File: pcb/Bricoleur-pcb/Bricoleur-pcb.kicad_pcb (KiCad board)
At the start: 2 copper layers, 74 parts, among them J1 USB_B_Micro, J2 Conn_02x10_Odd_Even, J3 Conn_02x03_Odd_Even, J4 Conn_02x03_Odd_Even, SW2 SW_Push, SW3 SW_Push, SW4 SW_Push, SW5 SW_Push, U1 Ultrasonic-LV-EZ0, U11 SW_DP3T, U2 PYNQ-Shield-Bricoleur-pcb-cac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, U3 Ultrasonic-LV-EZ0, U4 Ultrasonic-LV-EZ0, U5 Arducam-OV5642, U6 Arducam-OV5642, U7 EFM32GG980, U8 UART_BOOT, U9 IP4220CZ6

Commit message: Narrowed down component placement, continued routing
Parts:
- moved TP1 239.7 mm to (86.3, 158.6)
- moved U11 189.6 mm to (77.7, 141.9)
- moved C14 147.8 mm to (44.2, 155.6), turned to 90 degrees
- moved C15 142.5 mm to (60.4, 155.6), turned to 90 degrees
- moved C13 138.9 mm to (47.3, 109.4), turned to 180 degrees
- moved C16 138.0 mm to (77.7, 155.6), turned to 90 degrees
- moved L1 135.5 mm to (99.0, 90.1)
- moved J1 133.3 mm to (98.9, 95.3), turned to 270 degrees
- moved U9 129.6 mm to (104.1, 88.0)
- moved R4 121.2 mm to (68.1, 150.0), turned to 180 degrees
- moved C7 118.8 mm to (62.0, 126.1), turned to 270 degrees
- moved C9 117.2 mm to (56.4, 126.1), turned to 270 degrees
- moved C10 116.4 mm to (48.3, 111.4), turned to 180 degrees
- moved C3 111.8 mm to (57.9, 126.1), turned to 90 degrees
- moved R17 109.7 mm to (92.4, 143.4), turned to 270 degrees
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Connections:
- net Net-(J1-Pad2) renamed /USB_D-
- net Net-(J1-Pad3) renamed /USB_D+
- J1 pad 4: (no net) -> Net-(J1-Pad4)
- J2 pad 2: (no net) -> Net-(J2-Pad2)
- J2 pad 3: (no net) -> Net-(J2-Pad3)
- J2 pad 5: (no net) -> Net-(J2-Pad5)
- J3 pad 1: /US0_CLK -> /US0_TX
- J3 pad 5: /US0_TX -> /US0_CLK
- J4 pad 1: /US1_CLK -> /US1_TX
- J4 pad 5: /US1_TX -> /US1_CLK
- U1 pad 2: (no net) -> Net-(U1-Pad2)
- U1 pad 4: (no net) -> Net-(U1-Pad4)
- U2 pad 1: (no net) -> Net-(U2-Pad1)
- U2 pad 10: (no net) -> Net-(U2-Pad10)
- U2 pad 11: (no net) -> Net-(U2-Pad11)
- U2 pad 12: (no net) -> Net-(U2-Pad12)
- U2 pad 13: (no net) -> Net-(U2-Pad13)
- U2 pad 14: (no net) -> Net-(U2-Pad14)
- U2 pad 15: (no net) -> Net-(U2-Pad15)
- U2 pad 16: (no net) -> Net-(U2-Pad16)
- U2 pad 17: (no net) -> Net-(U2-Pad17)
- U2 pad 18: (no net) -> Net-(U2-Pad18)
- U2 pad 19: (no net) -> Net-(U2-Pad19)
- U2 pad 2: (no net) -> Net-(U2-Pad2)
- U2 pad 20: (no net) -> Net-(U2-Pad20)
- U2 pad 21: (no net) -> Net-(U2-Pad21)
- U2 pad 22: (no net) -> Net-(U2-Pad22)
- U2 pad 23: (no net) -> Net-(U2-Pad23)
- U2 pad 24: (no net) -> Net-(U2-Pad24)
- U2 pad 25: (no net) -> Net-(U2-Pad25)
- U2 pad 26: (no net) -> Net-(U2-Pad26)
- U2 pad 28: (no net) -> Net-(U2-Pad28)
- U2 pad 3: (no net) -> Net-(U2-Pad3)
- U2 pad 34: (no net) -> Net-(U2-Pad34)
- U2 pad 5: (no net) -> /PYNQ_5V0
- U2 pad 8: (no net) -> Net-(U2-Pad8)
- U2 pad 9: (no net) -> Net-(U2-Pad9)
- U3 pad 2: (no net) -> Net-(U3-Pad2)
- U3 pad 4: (no net) -> Net-(U3-Pad4)
- U4 pad 2: (no net) -> Net-(U4-Pad2)
- U4 pad 4: (no net) -> Net-(U4-Pad4)
- U5 pad 18: (no net) -> Net-(U5-Pad18)
- U5 pad 19: (no net) -> Net-(U5-Pad19)
- U5 pad 20: (no net) -> Net-(U5-Pad20)
- U6 pad 18: (no net) -> Net-(U6-Pad18)
- U6 pad 19: (no net) -> Net-(U6-Pad19)
- U6 pad 20: (no net) -> Net-(U6-Pad20)
- U7 pad 100: (no net) -> Net-(U7-Pad100)
- U7 pad 11: (no net) -> Net-(U7-Pad11)
- U7 pad 12: (no net) -> Net-(U7-Pad12)
- U7 pad 13: (no net) -> Net-(U7-Pad13)
- U7 pad 14: (no net) -> Net-(U7-Pad14)
- U7 pad 15: (no net) -> Net-(U7-Pad15)
- U7 pad 2: (no net) -> Net-(U7-Pad2)
- U7 pad 20: (no net) -> Net-(U7-Pad20)
- U7 pad 21: (no net) -> Net-(U7-Pad21)
- U7 pad 22: (no net) -> Net-(U7-Pad22)
- U7 pad 23: (no net) -> Net-(U7-Pad23)
- U7 pad 25: (no net) -> Net-(U7-Pad25)
- U7 pad 26: (no net) -> Net-(U7-Pad26)
- U7 pad 27: (no net) -> Net-(U7-Pad27)
- U7 pad 28: (no net) -> Net-(U7-Pad28)
- U7 pad 29: (no net) -> Net-(U7-Pad29)
- U7 pad 3: (no net) -> Net-(U7-Pad3)
- U7 pad 30: (no net) -> Net-(U7-Pad30)
- U7 pad 32: (no net) -> /VSS07
- U7 pad 33: (no net) -> Net-(U7-Pad33)
- U7 pad 34: (no net) -> Net-(U7-Pad34)
- U7 pad 35: (no net) -> Net-(U7-Pad35)
- U7 pad 40: (no net) -> Net-(U7-Pad40)
- U7 pad 42: (no net) -> Net-(U7-Pad42)
- U7 pad 43: (no net) -> Net-(U7-Pad43)
- U7 pad 46: (no net) -> Net-(U7-Pad46)
- U7 pad 47: (no net) -> Net-(U7-Pad47)
- U7 pad 48: (no net) -> Net-(U7-Pad48)
- U7 pad 49: (no net) -> Net-(U7-Pad49)
- U7 pad 50: (no net) -> Net-(U7-Pad50)
- U7 pad 51: (no net) -> Net-(U7-Pad51)
- U7 pad 52: (no net) -> Net-(U7-Pad52)
- U7 pad 53: (no net) -> Net-(U7-Pad53)
- U7 pad 54: (no net) -> Net-(U7-Pad54)
- U7 pad 55: (no net) -> Net-(U7-Pad55)
- U7 pad 56: (no net) -> Net-(U7-Pad56)
- U7 pad 60: (no net) -> Net-(U7-Pad60)
- U7 pad 61: (no net) -> Net-(U7-Pad61)
- U7 pad 65: (no net) -> Net-(U7-Pad65)
- U7 pad 66: (no net) -> Net-(U7-Pad66)
- U7 pad 67: (no net) -> Net-(U7-Pad67)
- U7 pad 68: (no net) -> Net-(U7-Pad68)
- U7 pad 7: (no net) -> Net-(U7-Pad7)
- U7 pad 80: (no net) -> Net-(U7-Pad80)
- U7 pad 81: (no net) -> Net-(U7-Pad81)
- U7 pad 84: (no net) -> Net-(U7-Pad84)
- U7 pad 85: (no net) -> Net-(U7-Pad85)
- U7 pad 86: (no net) -> Net-(U7-Pad86)
- U7 pad 87: (no net) -> Net-(U7-Pad87)
- U7 pad 88: (no net) -> Net-(U7-Pad88)
- U7 pad 89: (no net) -> Net-(U7-Pad89)
- U7 pad 9: (no net) -> Net-(U7-Pad9)
- U7 pad 90: (no net) -> Net-(U7-Pad90)
- U7 pad 91: (no net) -> Net-(U7-Pad91)
- U7 pad 92: (no net) -> Net-(U7-Pad92)
- U7 pad 93: (no net) -> Net-(U7-Pad93)
- U7 pad 96: (no net) -> Net-(U7-Pad96)
- U7 pad 97: (no net) -> Net-(U7-Pad97)
- U7 pad 98: (no net) -> Net-(U7-Pad98)
- U7 pad 99: (no net) -> Net-(U7-Pad99)
- U9 pad 1: (no net) -> Net-(U9-Pad1)
- U9 pad 3: (no net) -> Net-(U9-Pad3)
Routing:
- net /US0_CLK: track 9.17 -> 47.3 mm
- net /US0_TX: track 9.37 -> 47.3 mm
- net /US0_RX: track 8.96 -> 46.6 mm
- net GND: track 157.4 -> 179.2 mm
- net /sheet5BB7B6EA/INP: track 9.47 -> 22.2 mm
- net /Sheet5BB71F0E/INP: track 9.34 -> 21.2 mm
- net DH_TCK_SWCLK: track 18.9 -> 29.2 mm
- net Net-(C1-Pad2): track 0.00 -> 10.2 mm
- net VMCU: track 102.3 -> 111.9 mm
- net /AVDDU7: track 0.00 -> 8.80 mm
- net Net-(C2-Pad2): track 0.00 -> 8.44 mm
- net DBG_PB_3: track 13.4 -> 21.7 mm
- net DBG_PB_2: track 13.4 -> 21.5 mm
- net DBG_PB_1: track 13.5 -> 21.1 mm
- net Net-(C4-Pad2): track 0.00 -> 5.32 mm
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
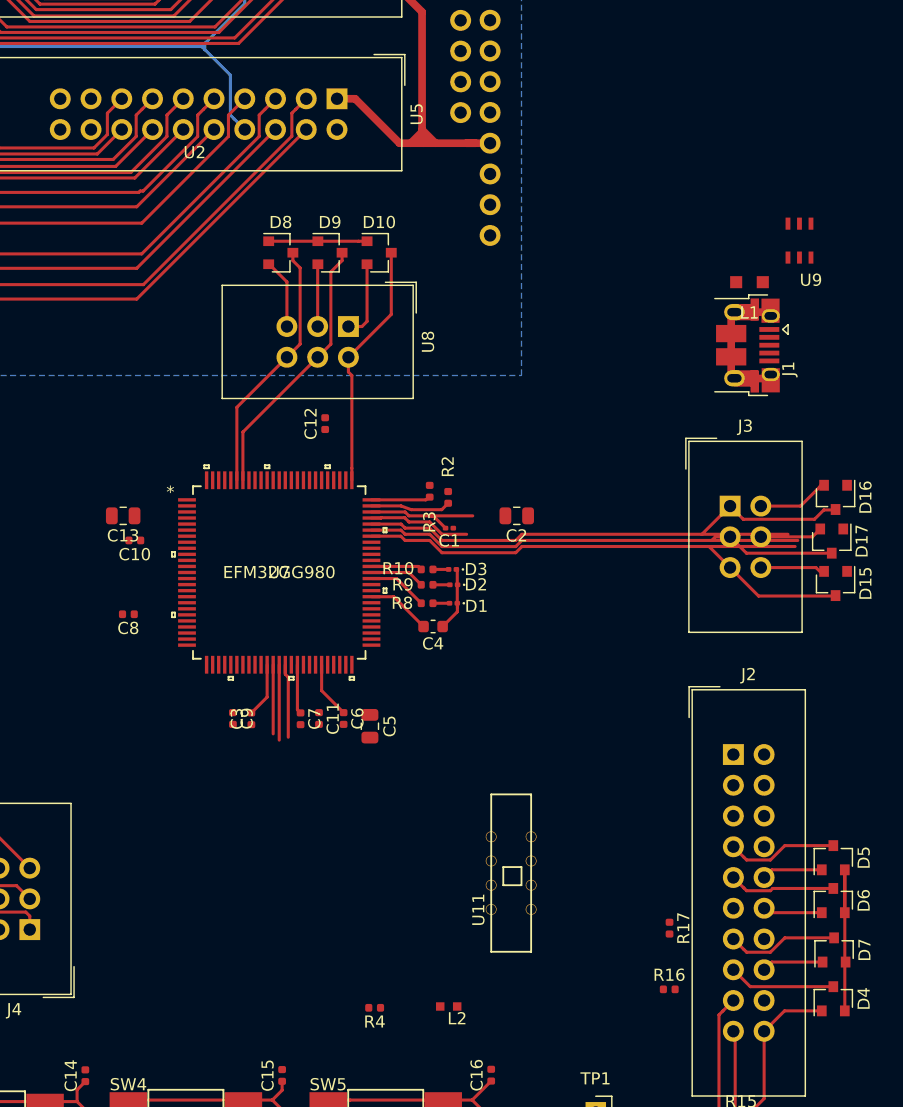
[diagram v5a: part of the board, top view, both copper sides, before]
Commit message: Power and clock networks ready (probably).
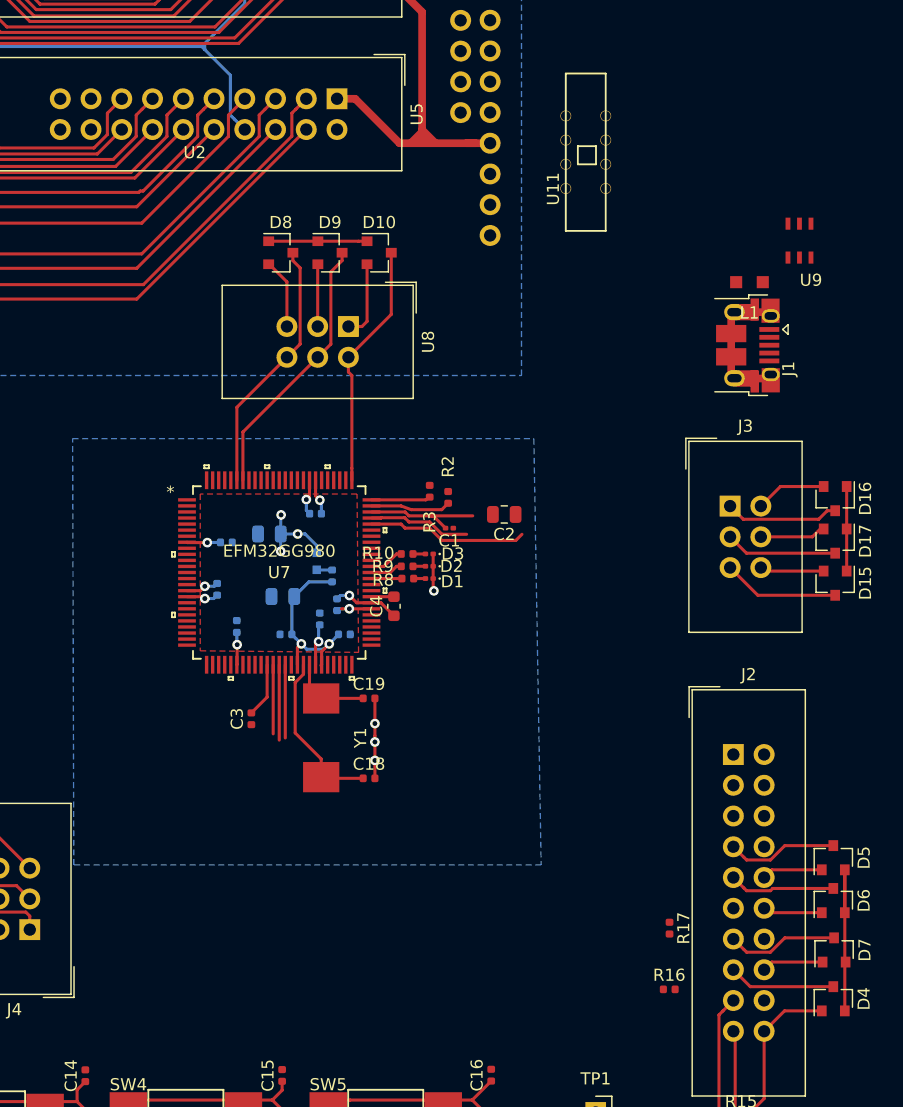
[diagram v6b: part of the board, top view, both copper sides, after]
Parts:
- added C17: 100N, Capacitor_SMD:C_0402_1005Metric, B.Cu at (56.7, 118.5)
- added C18: 27p, Capacitor_SMD:C_0402_1005Metric, F.Cu at (67.6, 131.0)
- added C19: 27p, Capacitor_SMD:C_0402_1005Metric, F.Cu at (67.6, 124.4)
- added Y1: ABM2-48.000MHZ-D4YF-T, XTAL:XTAL, F.Cu at (63.9, 128.0)
- C10, C11, C12, C13, C5, C6, C7, C8, C9, L2, R4: moved to B.Cu
- moved U11 59.9 mm to (83.9, 82.3)
- moved L2 39.2 mm to (63.3, 112.4), turned to 270 degrees
- moved R4 35.8 mm to (64.6, 114.3), turned to 270 degrees
- moved C10 16.6 mm to (63.5, 117.9), turned to 90 degrees
- moved C11 13.6 mm to (55.1, 115.4), turned to 90 degrees
- moved C5 12.9 mm to (60.5, 116.0), turned to 180 degrees
- moved C9 12.7 mm to (65.0, 116.7), turned to 90 degrees
- moved C13 12.2 mm to (59.4, 110.9)
- moved C8 10.0 mm to (55.8, 111.6), turned to 0 degrees
- moved C6 8.43 mm to (60.8, 119.2), turned to 180 degrees
- moved C7 7.86 mm to (65.6, 119.2), turned to 0 degrees
- moved C12 7.48 mm to (63.2, 109.2), turned to 180 degrees
- moved C4 3.64 mm to (69.7, 116.8), turned to 90 degrees
- moved D1 2.85 mm to (72.6, 114.5)
- moved R8 2.59 mm to (70.8, 114.5)
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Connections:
- J1 pad 4: Net-(J1-Pad4) -> (no net)
- J2 pad 2: Net-(J2-Pad2) -> (no net)
- J2 pad 3: Net-(J2-Pad3) -> (no net)
- J2 pad 5: Net-(J2-Pad5) -> (no net)
- U1 pad 2: Net-(U1-Pad2) -> (no net)
- U1 pad 4: Net-(U1-Pad4) -> (no net)
- U2 pad 1: Net-(U2-Pad1) -> (no net)
- U2 pad 10: Net-(U2-Pad10) -> (no net)
- U2 pad 11: Net-(U2-Pad11) -> (no net)
- U2 pad 12: Net-(U2-Pad12) -> (no net)
- U2 pad 13: Net-(U2-Pad13) -> (no net)
- U2 pad 14: Net-(U2-Pad14) -> (no net)
- U2 pad 15: Net-(U2-Pad15) -> (no net)
- U2 pad 16: Net-(U2-Pad16) -> (no net)
- U2 pad 17: Net-(U2-Pad17) -> (no net)
- U2 pad 18: Net-(U2-Pad18) -> (no net)
- U2 pad 19: Net-(U2-Pad19) -> (no net)
- U2 pad 2: Net-(U2-Pad2) -> (no net)
- U2 pad 20: Net-(U2-Pad20) -> (no net)
- U2 pad 21: Net-(U2-Pad21) -> (no net)
- U2 pad 22: Net-(U2-Pad22) -> (no net)
- U2 pad 23: Net-(U2-Pad23) -> (no net)
- U2 pad 24: Net-(U2-Pad24) -> (no net)
- U2 pad 25: Net-(U2-Pad25) -> (no net)
- U2 pad 26: Net-(U2-Pad26) -> (no net)
- U2 pad 28: Net-(U2-Pad28) -> (no net)
- U2 pad 3: Net-(U2-Pad3) -> (no net)
- U2 pad 34: Net-(U2-Pad34) -> (no net)
- U2 pad 5: /PYNQ_5V0 -> (no net)
- U2 pad 8: Net-(U2-Pad8) -> (no net)
- U2 pad 9: Net-(U2-Pad9) -> (no net)
- U3 pad 2: Net-(U3-Pad2) -> (no net)
- U3 pad 4: Net-(U3-Pad4) -> (no net)
- U4 pad 2: Net-(U4-Pad2) -> (no net)
- U4 pad 4: Net-(U4-Pad4) -> (no net)
- U5 pad 18: Net-(U5-Pad18) -> (no net)
- U5 pad 19: Net-(U5-Pad19) -> (no net)
- U5 pad 20: Net-(U5-Pad20) -> (no net)
- U6 pad 18: Net-(U6-Pad18) -> (no net)
- U6 pad 19: Net-(U6-Pad19) -> (no net)
- U6 pad 20: Net-(U6-Pad20) -> (no net)
- U7 pad 100: Net-(U7-Pad100) -> (no net)
- U7 pad 11: Net-(U7-Pad11) -> (no net)
- U7 pad 12: Net-(U7-Pad12) -> (no net)
- U7 pad 13: Net-(U7-Pad13) -> (no net)
- U7 pad 14: Net-(U7-Pad14) -> (no net)
- U7 pad 15: Net-(U7-Pad15) -> (no net)
- U7 pad 2: Net-(U7-Pad2) -> (no net)
- U7 pad 20: Net-(U7-Pad20) -> (no net)
- U7 pad 21: Net-(U7-Pad21) -> (no net)
- U7 pad 22: Net-(U7-Pad22) -> (no net)
- U7 pad 23: Net-(U7-Pad23) -> (no net)
- U7 pad 25: Net-(U7-Pad25) -> (no net)
- U7 pad 26: Net-(U7-Pad26) -> (no net)
- U7 pad 27: Net-(U7-Pad27) -> (no net)
- U7 pad 28: Net-(U7-Pad28) -> (no net)
- U7 pad 29: Net-(U7-Pad29) -> (no net)
- U7 pad 3: Net-(U7-Pad3) -> (no net)
- U7 pad 30: Net-(U7-Pad30) -> (no net)
- U7 pad 32: /VSS07 -> (no net)
- U7 pad 33: Net-(U7-Pad33) -> (no net)
- U7 pad 34: Net-(U7-Pad34) -> (no net)
- U7 pad 35: Net-(U7-Pad35) -> (no net)
- U7 pad 40: Net-(U7-Pad40) -> (no net)
- U7 pad 46: Net-(U7-Pad46) -> (no net)
- U7 pad 47: Net-(U7-Pad47) -> (no net)
- U7 pad 48: Net-(U7-Pad48) -> (no net)
- U7 pad 49: Net-(U7-Pad49) -> (no net)
- U7 pad 50: Net-(U7-Pad50) -> (no net)
- U7 pad 51: Net-(U7-Pad51) -> (no net)
- U7 pad 52: Net-(U7-Pad52) -> (no net)
- U7 pad 53: Net-(U7-Pad53) -> (no net)
- U7 pad 54: Net-(U7-Pad54) -> (no net)
- U7 pad 55: Net-(U7-Pad55) -> (no net)
- U7 pad 56: Net-(U7-Pad56) -> (no net)
- U7 pad 60: Net-(U7-Pad60) -> (no net)
- U7 pad 61: Net-(U7-Pad61) -> (no net)
- U7 pad 65: Net-(U7-Pad65) -> (no net)
- U7 pad 66: Net-(U7-Pad66) -> (no net)
- U7 pad 67: Net-(U7-Pad67) -> (no net)
- U7 pad 68: Net-(U7-Pad68) -> (no net)
- U7 pad 7: Net-(U7-Pad7) -> (no net)
- U7 pad 80: Net-(U7-Pad80) -> (no net)
- U7 pad 81: Net-(U7-Pad81) -> (no net)
- U7 pad 84: Net-(U7-Pad84) -> (no net)
- U7 pad 85: Net-(U7-Pad85) -> (no net)
- U7 pad 86: Net-(U7-Pad86) -> (no net)
- U7 pad 87: Net-(U7-Pad87) -> (no net)
- U7 pad 88: Net-(U7-Pad88) -> (no net)
- U7 pad 89: Net-(U7-Pad89) -> (no net)
- U7 pad 9: Net-(U7-Pad9) -> (no net)
- U7 pad 90: Net-(U7-Pad90) -> (no net)
- U7 pad 91: Net-(U7-Pad91) -> (no net)
- U7 pad 92: Net-(U7-Pad92) -> (no net)
- U7 pad 93: Net-(U7-Pad93) -> (no net)
- U7 pad 96: Net-(U7-Pad96) -> (no net)
- U7 pad 97: Net-(U7-Pad97) -> (no net)
- U7 pad 98: Net-(U7-Pad98) -> (no net)
- U7 pad 99: Net-(U7-Pad99) -> (no net)
- U9 pad 1: Net-(U9-Pad1) -> (no net)
- U9 pad 3: Net-(U9-Pad3) -> (no net)
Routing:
- net /US0_RX: track 46.6 -> 8.96 mm
- net /US0_CLK: track 47.3 -> 9.63 mm
- net VMCU: track 111.9 -> 144.1 mm, vias 0 -> 9
- net /US0_TX: track 47.3 -> 22.6 mm
- net GND: track 179.2 -> 195.3 mm, vias 0 -> 7
- net Net-(C18-Pad1): track 0.00 -> 13.8 mm
- net /AVDDU7: track 8.80 -> 15.6 mm, vias 0 -> 2
- net Net-(C19-Pad1): track 0.00 -> 6.65 mm
- net Net-(C4-Pad2): track 5.32 -> 1.86 mm
- net DBG_LED_1: track 4.95 -> 2.51 mm
- net DBG_LED_2: track 4.53 -> 2.67 mm
- net DBG_LED_3: track 4.21 -> 2.89 mm
- net Net-(L2-Pad2): track 0.00 -> 1.28 mm
- added copper zone on F.Cu, net VMCU
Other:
- net class Power: trace_width 0.635 -> 0.254

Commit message: Routing sonars and AUX-UART
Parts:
- moved D14 44.6 mm to (52.6, 103.1), turned to 270 degrees
- moved C14 25.4 mm to (44.2, 181.0)
- moved C15 25.4 mm to (60.4, 181.0)
- moved C16 25.4 mm to (77.7, 181.0)
- moved R1 25.4 mm to (28.9, 187.1)
- moved R5 25.4 mm to (44.4, 184.6)
- moved R6 25.4 mm to (60.7, 184.6)
- moved R7 25.4 mm to (77.2, 184.6)
- moved SW2 25.4 mm to (26.2, 187.6)
- moved SW3 25.4 mm to (31.4, 183.2)
- moved SW4 25.4 mm to (47.7, 183.0)
- moved SW5 25.4 mm to (64.2, 183.0)
- moved TP1 25.4 mm to (86.3, 184.0)
- moved R11 25.4 mm to (44.4, 186.8)
- moved R12 25.4 mm to (60.7, 186.8)
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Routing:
- net /US1_RX: track 8.71 -> 39.7 mm
- net /US1_CLK: track 9.91 -> 40.5 mm
- net VMCU: track 144.1 -> 173.5 mm, vias 9 -> 12
- net /US1_TX: track 9.41 -> 34.9 mm
- net GND: track 195.3 -> 216.5 mm, vias 7 -> 12
- net /Ultra/RX2: track 10.1 -> 29.4 mm
- net PULSE: track 30.4 -> 49.3 mm
- net /Ultra/RX1: track 10.2 -> 20.2 mm
- net /Ultra/RX0: track 10.2 -> 18.9 mm

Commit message: Moar routing
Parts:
- moved D16 75.4 mm to (30.9, 102.8)
- moved D17 75.3 mm to (30.9, 107.9)
- moved D15 75.2 mm to (30.9, 113.0)
- moved J3 60.5 mm to (37.0, 106.3)
- moved C19 16.3 mm to (67.1, 140.7)
- moved C6 16.3 mm to (60.2, 135.4)
- moved C7 16.3 mm to (65.1, 135.4)
- moved C9 16.3 mm to (64.5, 133.0)
- moved D3 16.3 mm to (72.1, 128.8)
- moved R10 16.3 mm to (70.3, 128.8)
- moved R9 16.3 mm to (70.3, 129.8)
- moved C1 16.3 mm to (73.7, 126.6)
- moved C10 16.3 mm to (63.0, 134.1)
- moved C11 16.3 mm to (54.6, 131.7)
- moved C12 16.3 mm to (62.7, 125.4)
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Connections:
- U2 pad 43: /US0_CLK -> /US0_RX
- U2 pad 46: /US0_RX -> /US0_CLK
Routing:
- net /US0_CLK: track 9.63 -> 100.6 mm, vias 0 -> 1
- net /US0_TX: track 22.6 -> 103.7 mm, vias 0 -> 1
- net /US0_RX: track 8.96 -> 89.7 mm, vias 0 -> 1
- net /sheet5BB7B6EA/INP: track 22.2 -> 9.47 mm
- net /Sheet5BB71F0E/INP: track 21.2 -> 9.34 mm
- net DH_TCK_SWCLK: track 29.2 -> 19.9 mm
- net VMCU: track 173.5 -> 180.1 mm
- net GND: track 216.5 -> 210.4 mm
